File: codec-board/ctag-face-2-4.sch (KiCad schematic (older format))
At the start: 8 parts

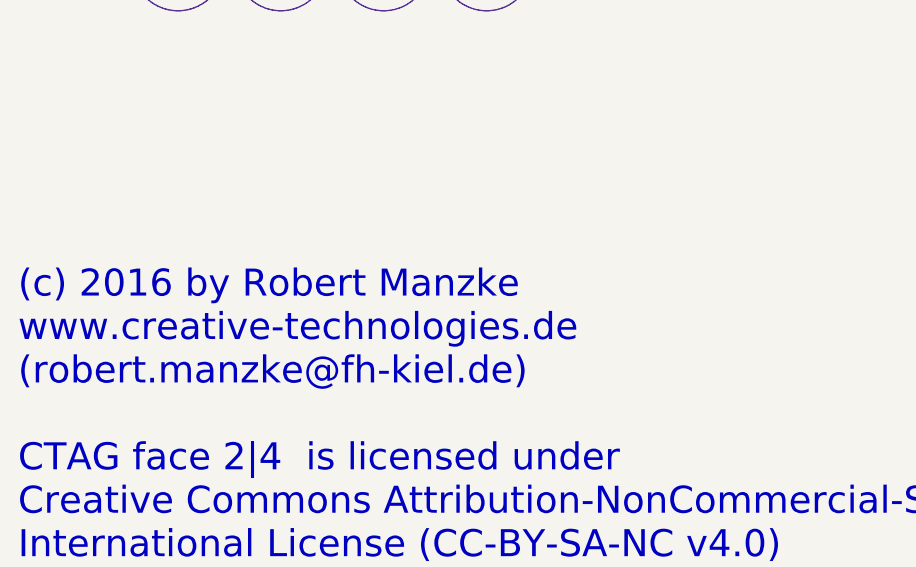
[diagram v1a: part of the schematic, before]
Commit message: fixed polarity bug on IN2
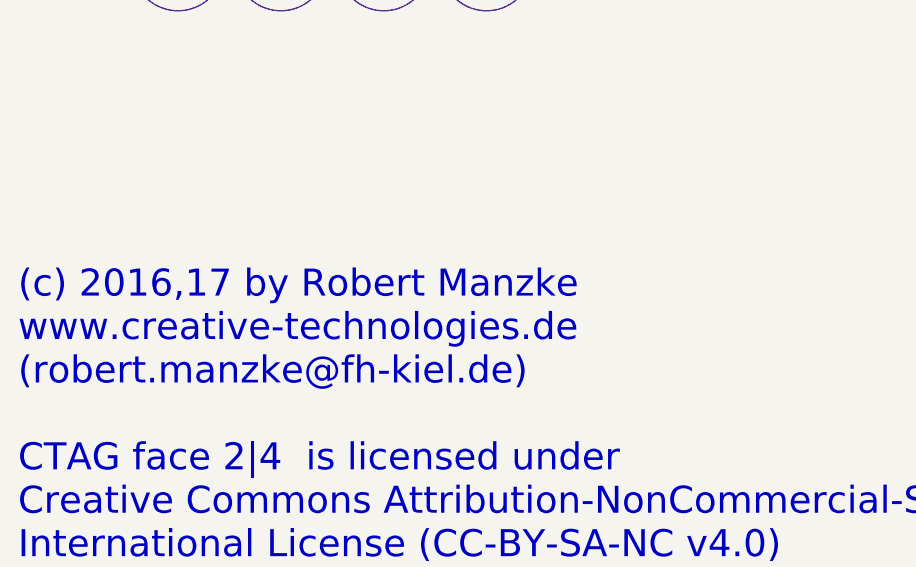
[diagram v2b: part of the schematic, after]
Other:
- note added: "(c) 2016,17 by Robert Manzke\nwww.creative-technologies.de \n(robert.manzke@fh-kiel.de)\n\nCTAG face 2|4 is licensed under \nCreative Commons Attribution-NonCommercial-ShareAlike 4.0 \nInternational License (CC-BY-SA-NC v4.0)\n\n"
- note removed: "(c) 2016 by Robert Manzke\nwww.creative-technologies.de \n(robert.manzke@fh-kiel.de)\n\nCTAG face 2|4 is licensed under \nCreative Commons Attribution-NonCommercial-ShareAlike 4.0 \nInternational License (CC-BY-SA-NC v4.0)\n\n"
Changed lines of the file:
@@
 Sheet 1 10
 Title "face 2|4"
-Date "2016"
-Rev "A"
+Date "2017"
+Rev "A2"
 Comp "www.creative-technologies.de"
 Comment1 "Robert Manzke"
@@
 $EndComp
 Text Notes 750  7600 0    118  ~ 0
-(c) 2016 by Robert Manzke\nwww.creative-technologies.de \n(robert.manzke@fh-kiel.de)\n\nCTAG face 2|4  is licensed under \nCreative Commons Attribution-NonCommercial-ShareAlike 4.0 \nInternational License (CC-BY-SA-NC v4.0)\n\n
+(c) 2016,17 by Robert Manzke\nwww.creative-technologies.de \n(robert.manzke@fh-kiel.de)\n\nCTAG face 2|4  is licensed under \nCreative Commons Attribution-NonCommercial-ShareAlike 4.0 \nInternational License (CC-BY-SA-NC v4.0)\n\n
 $EndSCHEMATC
